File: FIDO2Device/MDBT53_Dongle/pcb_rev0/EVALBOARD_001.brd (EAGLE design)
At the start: 45 x 45 mm, 47 parts, among them CN1 USB4105-GF-A, CN2 IF_6PIN, CN3 IF_7PIN, SW1 SKRPACE010, SW2 SKTADAE010, U1 MDBT53, U2 XC6206P332MR-G, U3 RV-3028-C7, X1 NX3215SA-32.768K-STD-MUA-9

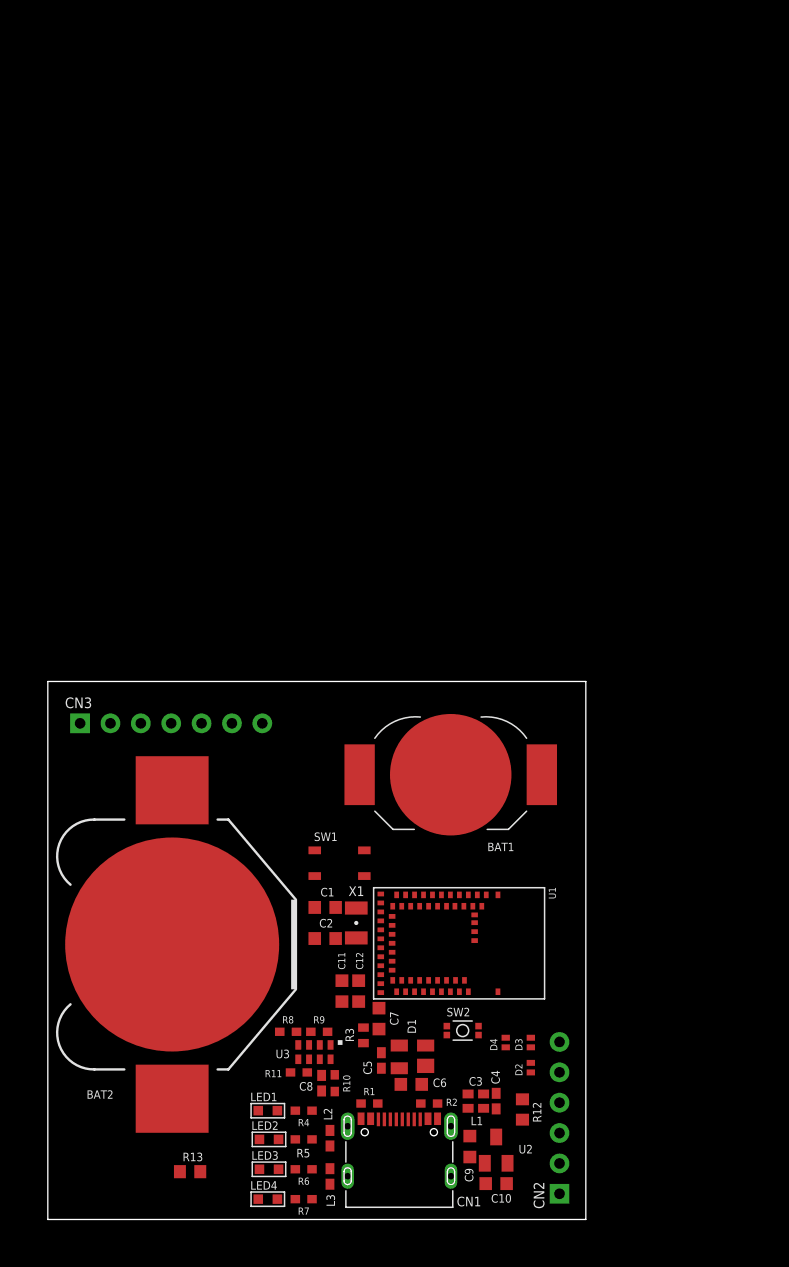
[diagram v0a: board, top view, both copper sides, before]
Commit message: 配線レイアウトを作成
・USB差動信号／CC／USB_GNDを配線
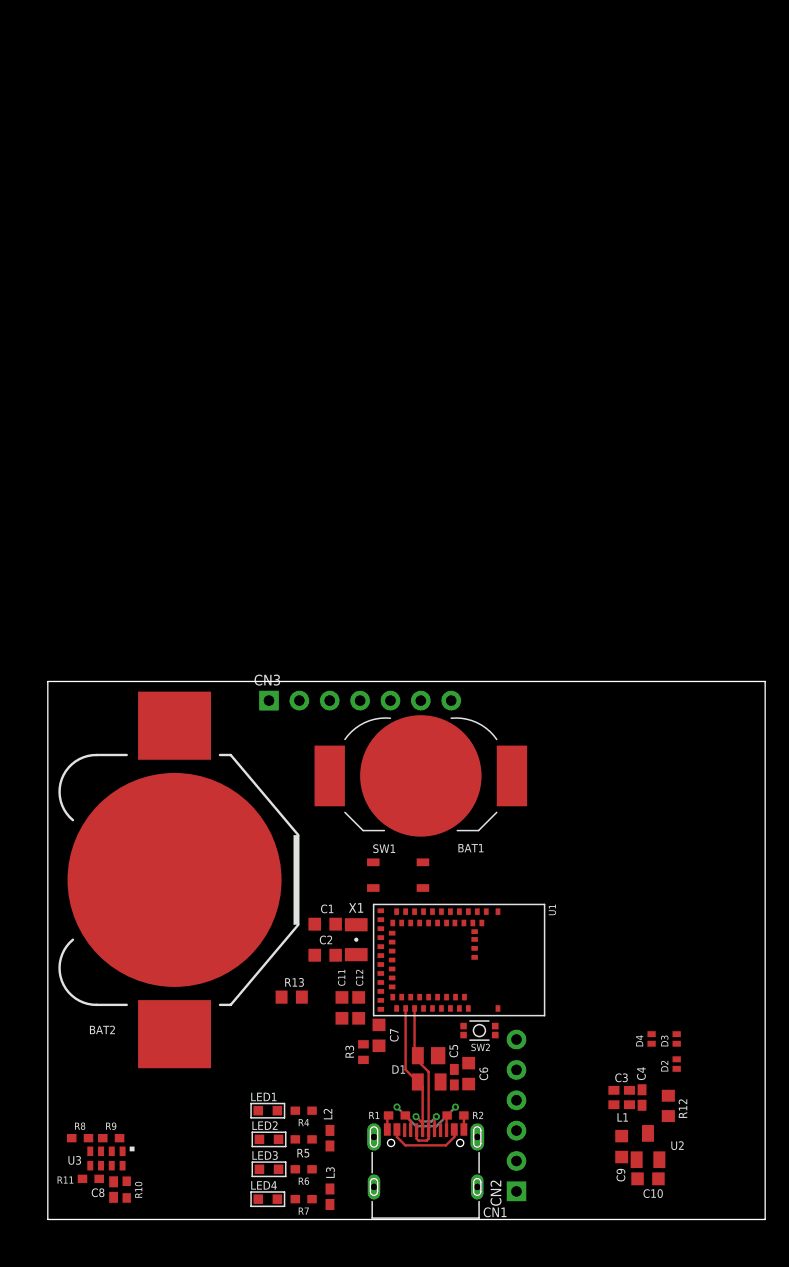
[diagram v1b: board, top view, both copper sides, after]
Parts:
- moved R8 19.5 mm to (2.70, 6.80)
- moved C8 19.5 mm to (5.50, 2.50)
- moved R10 19.5 mm to (6.60, 2.50)
- moved R11 19.5 mm to (3.60, 3.40)
- moved R9 19.5 mm to (5.30, 6.80)
- moved U3 19.5 mm to (6.50, 6.10)
- moved R13 16.9 mm to (20.4, 18.6)
- moved CN3 15.9 mm to (18.5, 43.4)
- moved C10 12.7 mm to (50.2, 3.40)
- moved U2 12.7 mm to (50.2, 6.10)
- moved C9 12.7 mm to (48.0, 6.10)
- moved C3 12.2 mm to (48.0, 10.8)
- moved C4 12.2 mm to (49.7, 10.2)
- moved D2 12.2 mm to (52.6, 13.0)
- moved D3 12.2 mm to (52.6, 15.1)
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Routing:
- net D_P: track 0.00 -> 15.8 mm, vias 0 -> 2
- net D_N: track 0.00 -> 13.2 mm
- net USB_GND: track 0.00 -> 8.62 mm, vias 0 -> 2
- net VBUS: track 0.00 -> 6.63 mm
- net N$2: track 0.00 -> 1.41 mm
- net N$3: track 0.00 -> 1.25 mm
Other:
- board size 45 x 45 mm -> 60 x 45 mm

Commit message: 配線レイアウトを作成
・ESDとVBUS／USB差動信号を配線
・基板右側の外形線を確定
・プログラム用I/F（スルーホール）を配置
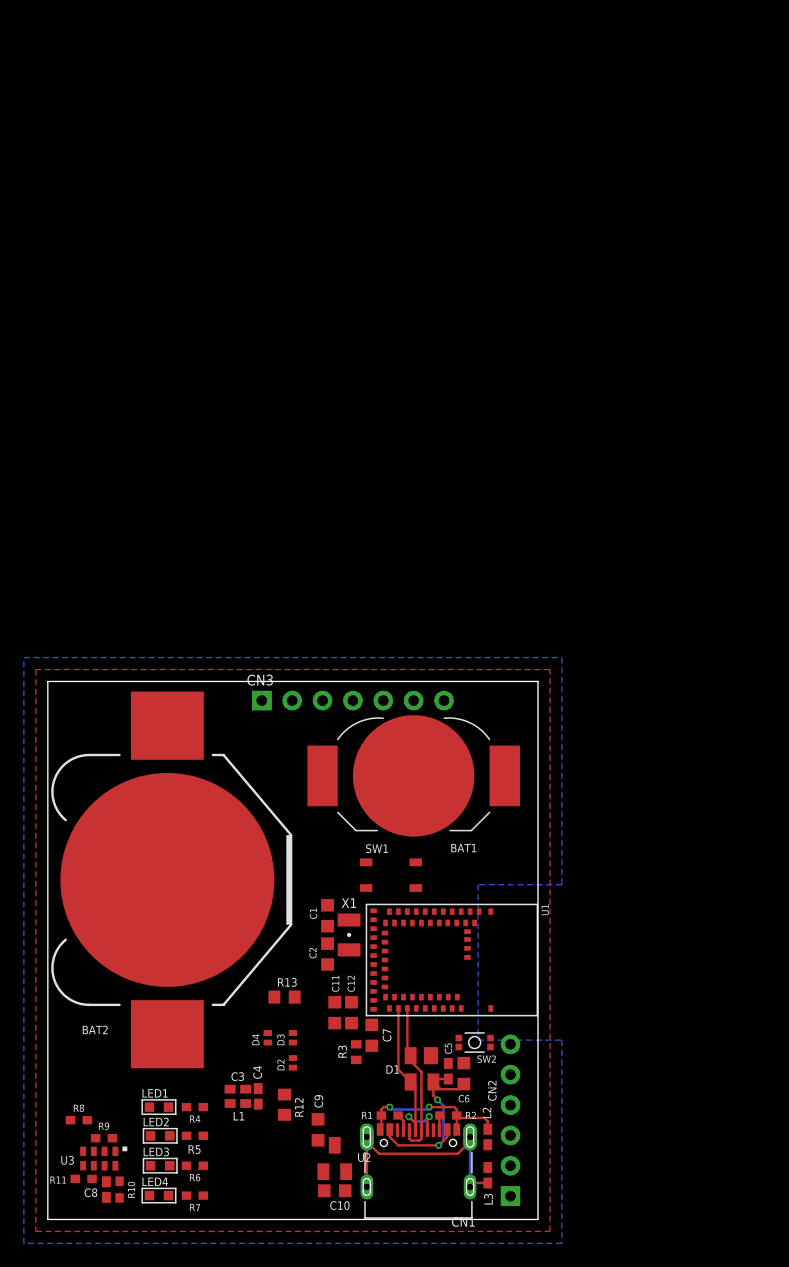
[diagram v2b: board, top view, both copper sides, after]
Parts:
- moved C3 32.1 mm to (15.9, 10.9)
- moved C4 32.1 mm to (17.6, 10.3)
- moved D2 32.1 mm to (20.5, 13.1)
- moved D3 32.1 mm to (20.5, 15.2)
- moved D4 32.1 mm to (18.4, 15.2)
- moved L1 32.1 mm to (15.9, 9.70)
- moved R12 32.1 mm to (19.8, 9.60)
- moved C10 26.2 mm to (24.0, 2.40)
- moved U2 26.2 mm to (24.0, 5.10)
- moved C9 25.4 mm to (22.6, 7.50), turned to 90 degrees
- moved L3 13.3 mm to (36.8, 3.70), turned to 90 degrees
- moved L2 13.2 mm to (36.8, 6.90)
- moved LED2 9.10 mm to (9.40, 7.00)
- moved LED3 9.10 mm to (9.40, 4.50)
- moved LED1 9.10 mm to (9.30, 9.40)
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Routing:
- net FG: track 0.00 -> 20.2 mm
- net VBUS: track 6.63 -> 16.8 mm, vias 0 -> 2
- net USB_GND: track 8.62 -> 13.5 mm
- added copper zone on layer 1, net 0V
- added copper zone on layer 16, net 0V
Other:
- board size 60 x 45 mm -> 41 x 45 mm

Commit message: 配線レイアウトを作成
・基板左側の外形線を確定
（これにより、基板サイズの幅が20mmに決まりました）
・電源平滑／降圧回路を配置
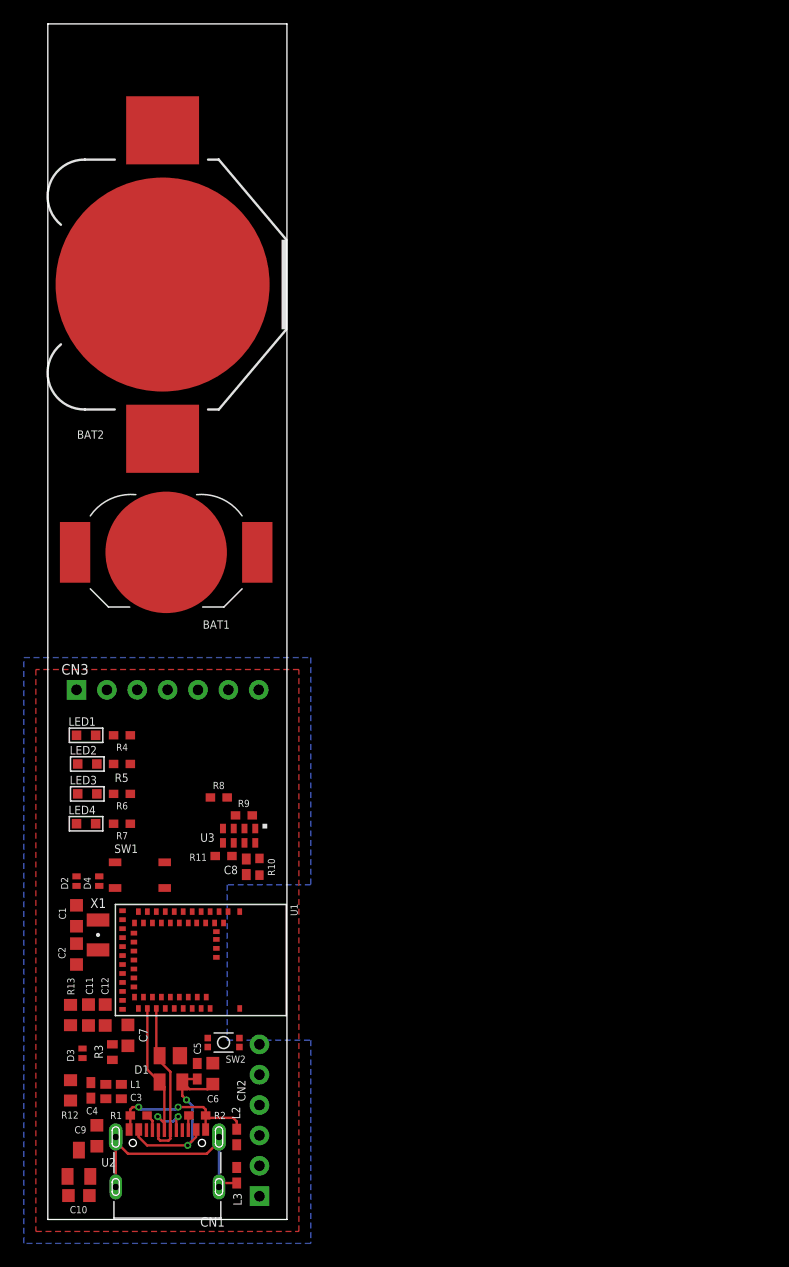
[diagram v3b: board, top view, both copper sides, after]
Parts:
- moved BAT2 49.8 mm to (9.60, 78.2)
- moved LED1 31.7 mm to (3.20, 40.5)
- moved LED2 31.7 mm to (3.30, 38.1)
- moved LED3 31.7 mm to (3.30, 35.6)
- moved LED4 31.7 mm to (3.20, 33.1)
- moved R4 31.7 mm to (6.20, 40.5)
- moved R5 31.7 mm to (6.20, 38.1)
- moved R6 31.7 mm to (6.20, 35.6)
- moved R7 31.7 mm to (6.20, 33.1)
- moved C8 29.4 mm to (16.6, 29.5)
- moved R10 29.4 mm to (17.7, 29.5)
- moved R11 29.4 mm to (14.7, 30.4)
- moved U3 29.4 mm to (17.6, 33.1)
- moved R8 29.4 mm to (14.3, 35.3)
- moved R9 29.4 mm to (16.4, 33.8)
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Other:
- board size 41 x 45 mm -> 20 x 100 mm
